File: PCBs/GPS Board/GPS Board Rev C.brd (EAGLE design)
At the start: 4 parts

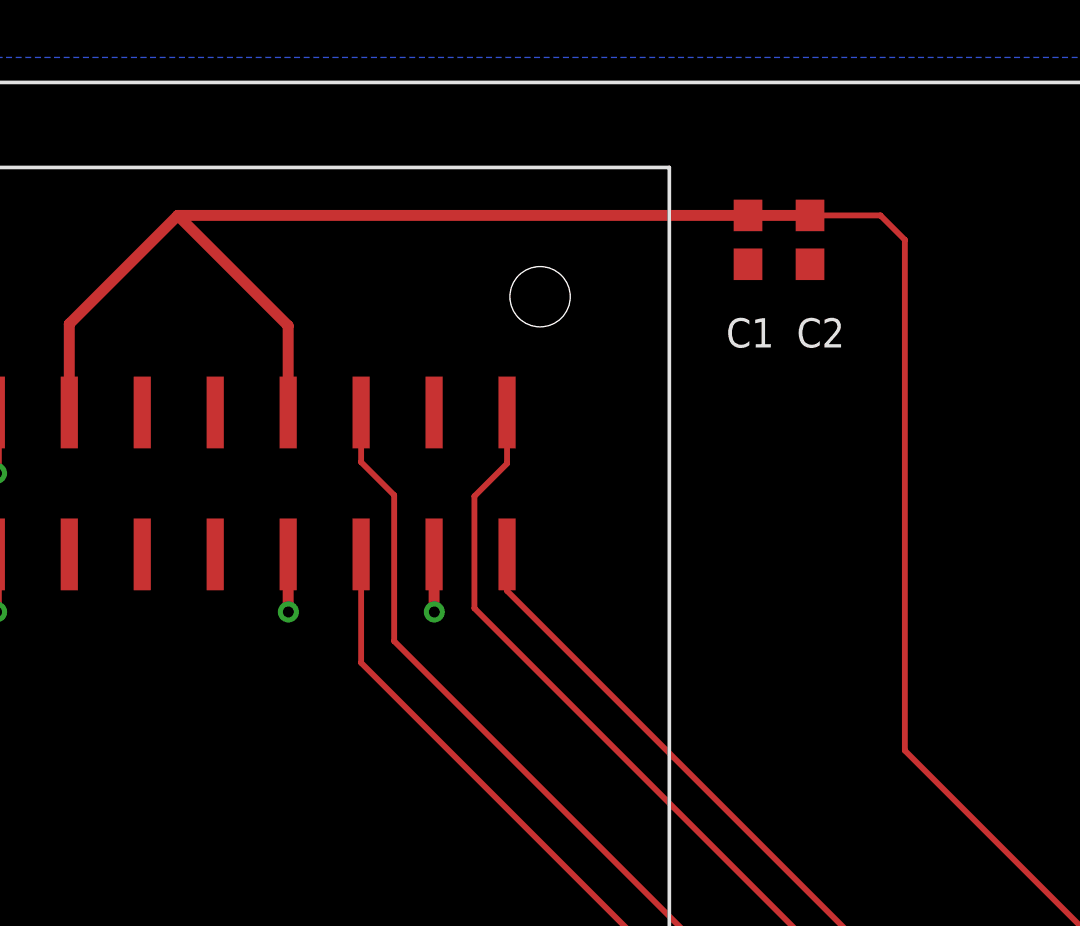
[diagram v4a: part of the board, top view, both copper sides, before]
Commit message: Replace components with 0805s
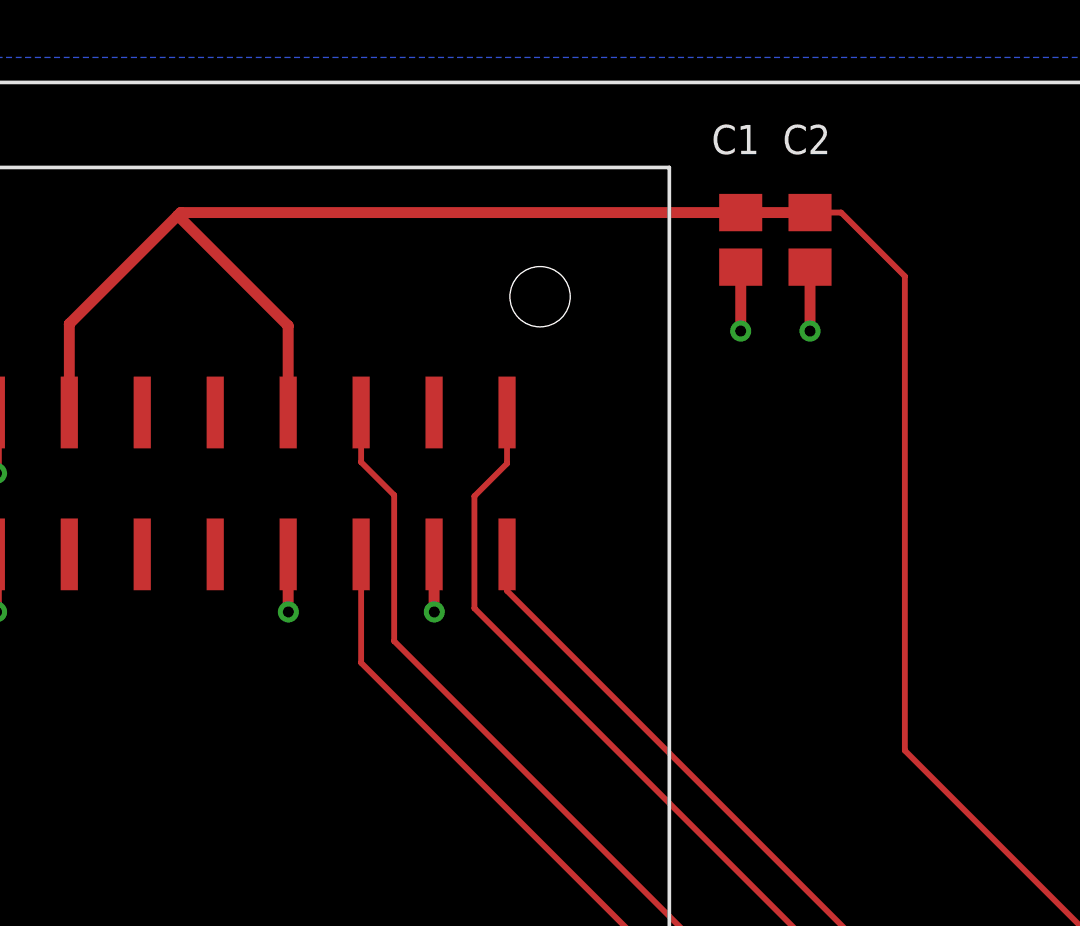
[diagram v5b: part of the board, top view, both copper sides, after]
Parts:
- C1, C2: device resistor:C0603 -> resistor:C0805
- moved C1 0.25 mm to (64.1, 85.1)
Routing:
- net GND: track 8.52 -> 13.0 mm, vias 4 -> 6
- net SW9: track 83.0 -> 82.3 mm
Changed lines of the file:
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@@
 <element name="U$1" library="pinavl1" package="PINAV-L1" value="PINAVL1" x="44.45" y="49.53" rot="R90"/>
 <element name="U$2" library="Cubesat" package="PC104" value="PC104" x="0" y="1.27"/>
-<element name="C2" library="resistor" library_urn="urn:adsk.eagle:library:348" package="C0603" package3d_urn="urn:adsk.eagle:package:26138/1" value="1uF" x="66.548" y="85.09" smashed="yes" rot="R270">
-<attribute name="NAME" x="67.7545" y="82.3595" size="1.016" layer="25" rot="R180"/>
-<attribute name="VALUE" x="66.167" y="80.391" size="0.635" layer="27"/>
+<element name="C2" library="resistor" library_urn="urn:adsk.eagle:library:348" package="C0805" package3d_urn="urn:adsk.eagle:package:26137/1" value="1uF" x="66.548" y="85.09" smashed="yes" rot="R270">
+<attribute name="NAME" x="65.5955" y="88.0745" size="1.016" layer="25"/>
+<attribute name="VALUE" x="65.786" y="87.249" size="0.635" layer="27"/>
 </element>
-<element name="C1" library="resistor" library_urn="urn:adsk.eagle:library:348" package="C0603" package3d_urn="urn:adsk.eagle:package:26138/1" value="0.1uF" x="64.389" y="85.09" smashed="yes" rot="R270">
-<attribute name="NAME" x="63.627" y="81.3435" size="1.016" layer="25"/>
-<attribute name="VALUE" x="63.373" y="80.264" size="0.635" layer="27"/>
+<element name="C1" library="resistor" library_urn="urn:adsk.eagle:library:348" package="C0805" package3d_urn="urn:adsk.eagle:package:26137/1" value="0.1uF" x="64.135" y="85.09" smashed="yes" rot="R270">
+<attribute name="NAME" x="63.119" y="88.0745" size="1.016" layer="25"/>
+<attribute name="VALUE" x="62.992" y="87.249" size="0.635" layer="27"/>
 </element>
 </elements>
@@
 <wire x1="44.538" y1="85.94" x2="48.38" y2="82.098" width="0.381" layer="1"/>
 <wire x1="48.38" y1="82.098" x2="48.38" y2="79.08" width="0.381" layer="1"/>
-<wire x1="66.548" y1="85.94" x2="64.389" y2="85.94" width="0.381" layer="1"/>
-<wire x1="64.389" y1="85.94" x2="44.538" y2="85.94" width="0.381" layer="1"/>
 <wire x1="87.23121875" y1="54.61" x2="85.96121875" y2="55.88" width="0.2032" layer="1"/>
 <wire x1="85.96121875" y1="55.88" x2="81.28" y2="55.88" width="0.2032" layer="1"/>
 <wire x1="81.28" y1="55.88" x2="69.85" y2="67.31" width="0.2032" layer="1"/>
-<wire x1="69.85" y1="85.09" x2="69" y2="85.94" width="0.2032" layer="1"/>
-<wire x1="69" y1="85.94" x2="66.548" y2="85.94" width="0.2032" layer="1"/>
-<wire x1="69.85" y1="67.31" x2="69.85" y2="85.09" width="0.2032" layer="1"/>
+<wire x1="69.85" y1="67.31" x2="69.85" y2="83.82" width="0.2032" layer="1"/>
+<wire x1="69.85" y1="83.82" x2="67.63" y2="86.04" width="0.2032" layer="1"/>
+<wire x1="67.63" y1="86.04" x2="66.548" y2="86.04" width="0.2032" layer="1"/>
+<wire x1="64.135" y1="86.04" x2="44.638" y2="86.04" width="0.381" layer="1"/>
+<wire x1="44.638" y1="86.04" x2="44.538" y2="85.94" width="0.381" layer="1"/>
+<wire x1="64.135" y1="86.04" x2="66.548" y2="86.04" width="0.381" layer="1"/>
 </signal>
 <signal name="GND">
@@
 <wire x1="53.46" y1="74.14" x2="53.34" y2="74.02" width="0.1524" layer="1"/>
 <wire x1="38.22" y1="79.08" x2="38.227" y2="79.2" width="0.1524" layer="1"/>
-<wire x1="66.4845" y1="84.1765" x2="66.548" y2="84.24" width="0.635" layer="1"/>
+<wire x1="66.4845" y1="84.1765" x2="66.548" y2="84.14" width="0.635" layer="1"/>
 <wire x1="48.38" y1="74.14" x2="48.38" y2="72.143" width="0.381" layer="1"/>
 <wire x1="48.38" y1="72.143" x2="48.387" y2="72.136" width="0.381" layer="1"/>
@@
 <wire x1="38.22" y1="72.143" x2="38.227" y2="72.136" width="0.381" layer="1"/>
 <via x="38.227" y="72.136" extent="1-16" drill="0.381"/>
-<wire x1="64.389" y1="84.24" x2="66.4845" y2="84.1765" width="0" layer="19" extent="1-1"/>
-<wire x1="53.46" y1="74.14" x2="64.389" y2="84.24" width="0" layer="19" extent="1-1"/>
+<wire x1="66.548" y1="84.14" x2="66.548" y2="81.915" width="0.381" layer="1"/>
+<via x="66.548" y="81.915" extent="1-16" drill="0.381"/>
+<wire x1="64.135" y1="84.14" x2="64.135" y2="81.915" width="0.381" layer="1"/>
+<via x="64.135" y="81.915" extent="1-16" drill="0.381"/>
 </signal>
 <signal name="VPP">

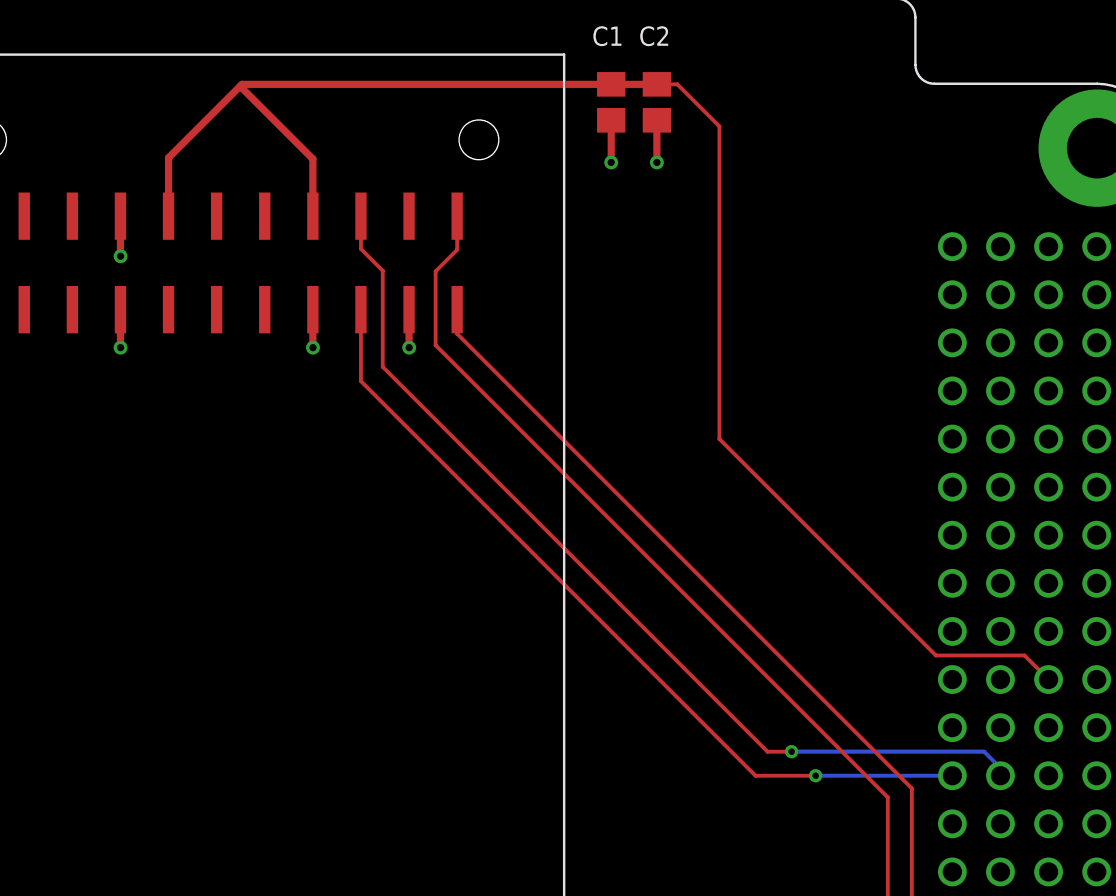
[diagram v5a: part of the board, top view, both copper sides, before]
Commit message: Make GPS board pass ERC and DRC
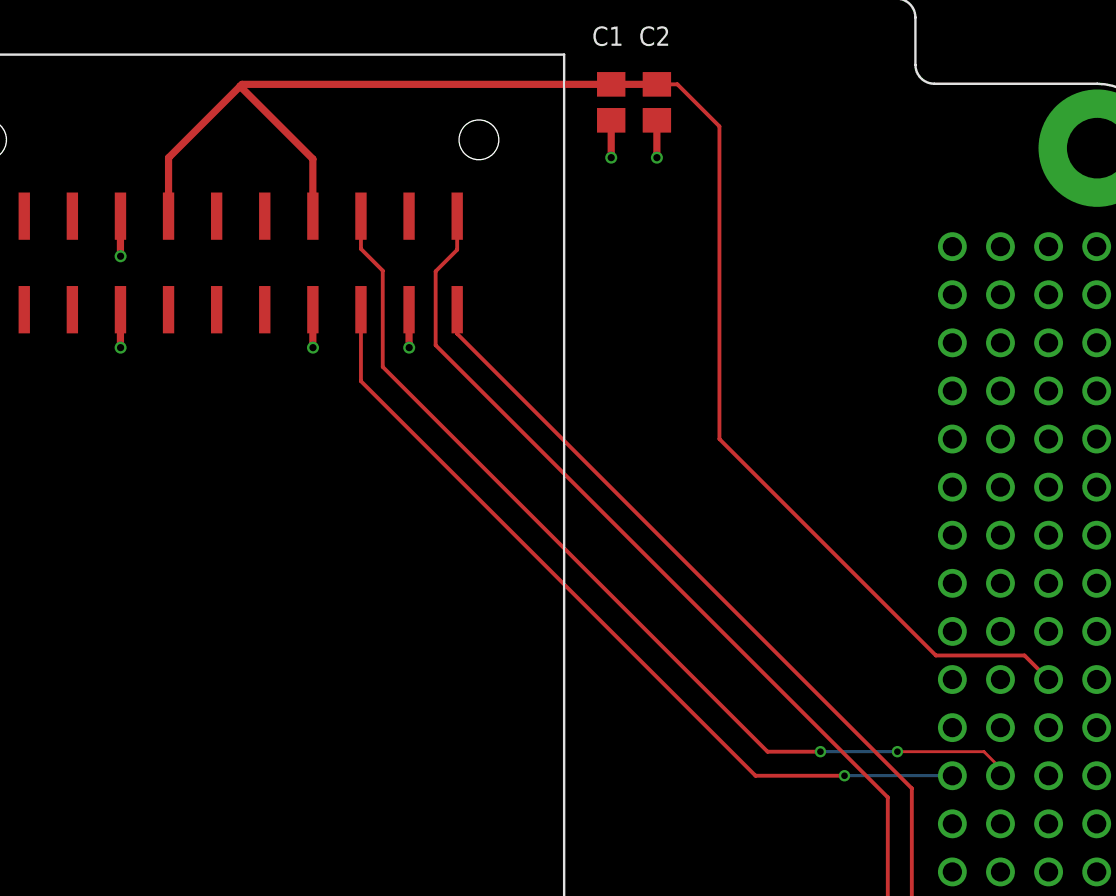
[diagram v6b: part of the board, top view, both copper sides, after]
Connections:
- removed net SW5: U$2.P$65
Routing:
- net GND: track 13.0 -> 12.1 mm
- net PF: vias 1 -> 2
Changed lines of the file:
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@@
 </classes>
 <designrules name="oshpark-2layer">
-<description language="de">&lt;b&gt;EAGLE Design Rules&lt;/b&gt;
+<description language="en">&lt;b&gt;OSH Park Design Rules&lt;/b&gt;
 &lt;p&gt;
-Die Standard-Design-Rules sind so gewählt, dass sie für
-die meisten Anwendungen passen. Sollte ihre Platine
-besondere Anforderungen haben, treffen Sie die erforderlichen
-Einstellungen hier und speichern die Design Rules unter
-einem neuen Namen ab.</description>
-<description language="en">&lt;b&gt;Laen's PCB Order Design Rules&lt;/b&gt;
+Please make sure your boards conform to these design rules.
+&lt;/p&gt;
 &lt;p&gt;
-Please make sure your boards conform to these design rules.</description>
+Note, that not all DRC settings must be set by the manufacturer. Several can be adjusted for the design, including those listed on our docs page here.
+&lt;a href=&quot;http://docs.oshpark.com/design-tools/eagle/design-rules-files/&quot;&gt;Adjustable Settings&lt;/a&gt;
+&lt;/p&gt;</description>
 <param name="layerSetup" value="(1*16)"/>
-<param name="mtCopper" value="0.0356mm 0.0356mm 0.0356mm 0.0356mm 0.0356mm 0.0356mm 0.0356mm 0.0356mm 0.0356mm 0.0356mm 0.0356mm 0.0356mm 0.0356mm 0.0356mm 0.0356mm 0.0356mm"/>
-<param name="mtIsolate" value="1.5011mm 0.1499mm 0.2007mm 0.1499mm 0.2007mm 0.1499mm 0.2007mm 0.1499mm 0.2007mm 0.1499mm 0.2007mm 0.1499mm 0.2007mm 0.1499mm 0.2007mm"/>
+<param name="mtCopper" value="0.035559375mm 0.0356mm 0.0356mm 0.0356mm 0.0356mm 0.0356mm 0.0356mm 0.0356mm 0.0356mm 0.0356mm 0.0356mm 0.0356mm 0.0356mm 0.0356mm 0.0356mm 0.035559375mm"/>
+<param name="mtIsolate" value="1.6mm 0.1499mm 0.2007mm 0.1499mm 0.2007mm 0.1499mm 0.2007mm 0.1499mm 0.2007mm 0.1499mm 0.2007mm 0.1499mm 0.2007mm 0.1499mm 0.2007mm"/>
 <param name="mdWireWire" value="6mil"/>
 <param name="mdWirePad" value="6mil"/>
@@
 <param name="mdSmdStop" value="0mil"/>
 <param name="msWidth" value="6mil"/>
-<param name="msDrill" value="13mil"/>
-<param name="msMicroVia" value="13mil"/>
+<param name="msDrill" value="10mil"/>
+<param name="msMicroVia" value="10mil"/>
 <param name="msBlindViaRatio" value="0.5"/>
 <param name="rvPadTop" value="0.25"/>
@@
 <param name="rvMicroViaOuter" value="0.25"/>
 <param name="rvMicroViaInner" value="0.25"/>
-<param name="rlMinPadTop" value="7mil"/>
+<param name="rlMinPadTop" value="5mil"/>
 <param name="rlMaxPadTop" value="20mil"/>
-<param name="rlMinPadInner" value="7mil"/>
+<param name="rlMinPadInner" value="5mil"/>
 <param name="rlMaxPadInner" value="20mil"/>
-<param name="rlMinPadBottom" value="7mil"/>
+<param name="rlMinPadBottom" value="5mil"/>
 <param name="rlMaxPadBottom" value="20mil"/>
-<param name="rlMinViaOuter" value="7mil"/>
+<param name="rlMinViaOuter" value="5mil"/>
 <param name="rlMaxViaOuter" value="20mil"/>
-<param name="rlMinViaInner" value="7mil"/>
+<param name="rlMinViaInner" value="5mil"/>
 <param name="rlMaxViaInner" value="20mil"/>
-<param name="rlMinMicroViaOuter" value="4mil"/>
+<param name="rlMinMicroViaOuter" value="5mil"/>
 <param name="rlMaxMicroViaOuter" value="20mil"/>
-<param name="rlMinMicroViaInner" value="4mil"/>
+<param name="rlMinMicroViaInner" value="5mil"/>
 <param name="rlMaxMicroViaInner" value="20mil"/>
 <param name="psTop" value="-1"/>
@@
 <contactref element="U$2" pad="P$73"/>
 <contactref element="U$2" pad="P$74"/>
-<wire x1="53.46" y1="74.14" x2="53.34" y2="74.02" width="0.1524" layer="1"/>
-<wire x1="38.22" y1="79.08" x2="38.227" y2="79.2" width="0.1524" layer="1"/>
-<wire x1="66.4845" y1="84.1765" x2="66.548" y2="84.14" width="0.635" layer="1"/>
 <wire x1="48.38" y1="74.14" x2="48.38" y2="72.143" width="0.381" layer="1"/>
 <wire x1="48.38" y1="72.143" x2="48.387" y2="72.136" width="0.381" layer="1"/>
@@
 <wire x1="38.22" y1="72.143" x2="38.227" y2="72.136" width="0.381" layer="1"/>
 <via x="38.227" y="72.136" extent="1-16" drill="0.381"/>
-<wire x1="66.548" y1="84.14" x2="66.548" y2="81.915" width="0.381" layer="1"/>
-<via x="66.548" y="81.915" extent="1-16" drill="0.381"/>
-<wire x1="64.135" y1="84.14" x2="64.135" y2="81.915" width="0.381" layer="1"/>
-<via x="64.135" y="81.915" extent="1-16" drill="0.381"/>
+<wire x1="66.548" y1="84.14" x2="66.548" y2="82.169" width="0.381" layer="1"/>
+<via x="66.548" y="82.169" extent="1-16" drill="0.381"/>
+<wire x1="64.135" y1="84.14" x2="64.135" y2="82.169" width="0.381" layer="1"/>
+<via x="64.135" y="82.169" extent="1-16" drill="0.381"/>
 </signal>
 <signal name="VPP">
@@
 <contactref element="U$2" pad="P$23"/>
 <wire x1="50.92" y1="74.14" x2="50.92" y2="70.365" width="0.2032" layer="1"/>
-<wire x1="71.755" y1="49.53" x2="74.93" y2="49.53" width="0.2032" layer="1"/>
-<via x="74.93" y="49.53" extent="1-16" drill="0.35"/>
-<wire x1="74.93" y1="49.53" x2="82.15121875" y2="49.53" width="0.2032" layer="16"/>
+<wire x1="71.755" y1="49.53" x2="76.454" y2="49.53" width="0.2032" layer="1"/>
+<via x="76.454" y="49.53" extent="1-16" drill="0.35"/>
 <wire x1="50.92" y1="70.365" x2="71.755" y2="49.53" width="0.2032" layer="1"/>
+<wire x1="82.15121875" y1="49.53" x2="76.454" y2="49.53" width="0.1524" layer="16"/>
 </signal>
 <signal name="PF">
@@
 <wire x1="52.07" y1="76.2" x2="52.07" y2="71.12" width="0.2032" layer="1"/>
 <wire x1="52.07" y1="71.12" x2="72.39" y2="50.8" width="0.2032" layer="1"/>
-<wire x1="72.39" y1="50.8" x2="73.66" y2="50.8" width="0.2032" layer="1"/>
-<via x="73.66" y="50.8" extent="1-16" drill="0.35"/>
-<wire x1="73.66" y1="50.8" x2="83.82" y2="50.8" width="0.2032" layer="16"/>
-<wire x1="83.82" y1="50.8" x2="84.69121875" y2="49.92878125" width="0.2032" layer="16"/>
-<wire x1="84.69121875" y1="49.92878125" x2="84.69121875" y2="49.53" width="0.2032" layer="16"/>
+<wire x1="72.39" y1="50.8" x2="75.184" y2="50.8" width="0.2032" layer="1"/>
+<via x="75.184" y="50.8" extent="1-16" drill="0.35"/>
+<wire x1="84.69121875" y1="49.53" x2="84.69121875" y2="49.92878125" width="0.1524" layer="1"/>
+<wire x1="84.69121875" y1="49.92878125" x2="83.82" y2="50.8" width="0.1524" layer="1"/>
+<wire x1="83.82" y1="50.8" x2="79.248" y2="50.8" width="0.1524" layer="1"/>
+<via x="79.248" y="50.8" extent="1-16" drill="0.35"/>
+<wire x1="79.248" y1="50.8" x2="75.184" y2="50.8" width="0.1524" layer="16"/>
 </signal>
 <signal name="TX">
@@
 <wire x1="56" y1="79.08" x2="56" y2="77.302" width="0.2032" layer="1"/>
 </signal>
-<signal name="SW5">
-<contactref element="U$2" pad="P$65"/>
-</signal>
 </signals>
